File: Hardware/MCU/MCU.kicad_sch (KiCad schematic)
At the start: 36 parts, among them J1 spi0, J10 i2s, J11 USB_C_Receptacle_USB2.0_16P, J2 sp1, J3 sp2, J4 1778612, J5 1778612, J6 1778612, J7 1778612, J8 i2c0, J9 i2c1, SW1 SW_Push, SW2 SW_Push, U1 ESP32-S3-WROOM-1, U2 USBLC6-2P6

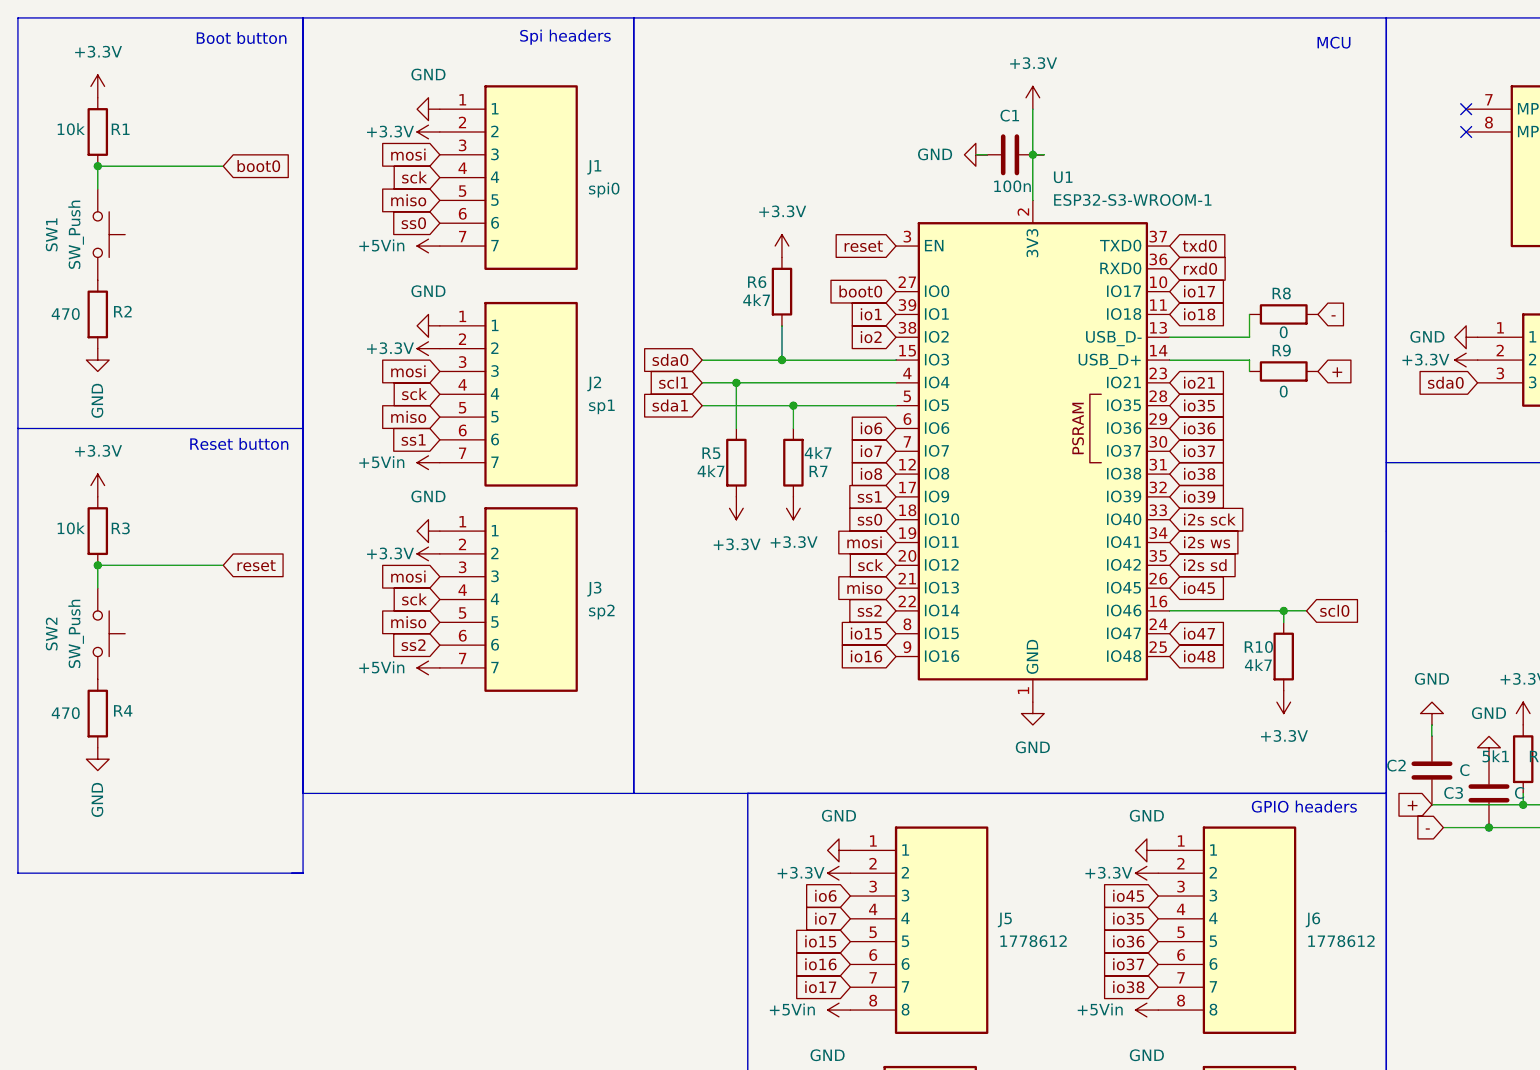
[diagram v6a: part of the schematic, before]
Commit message: boot en reset pin configuratie veranderd, pull up veranderd en capcitoren toegevoegd
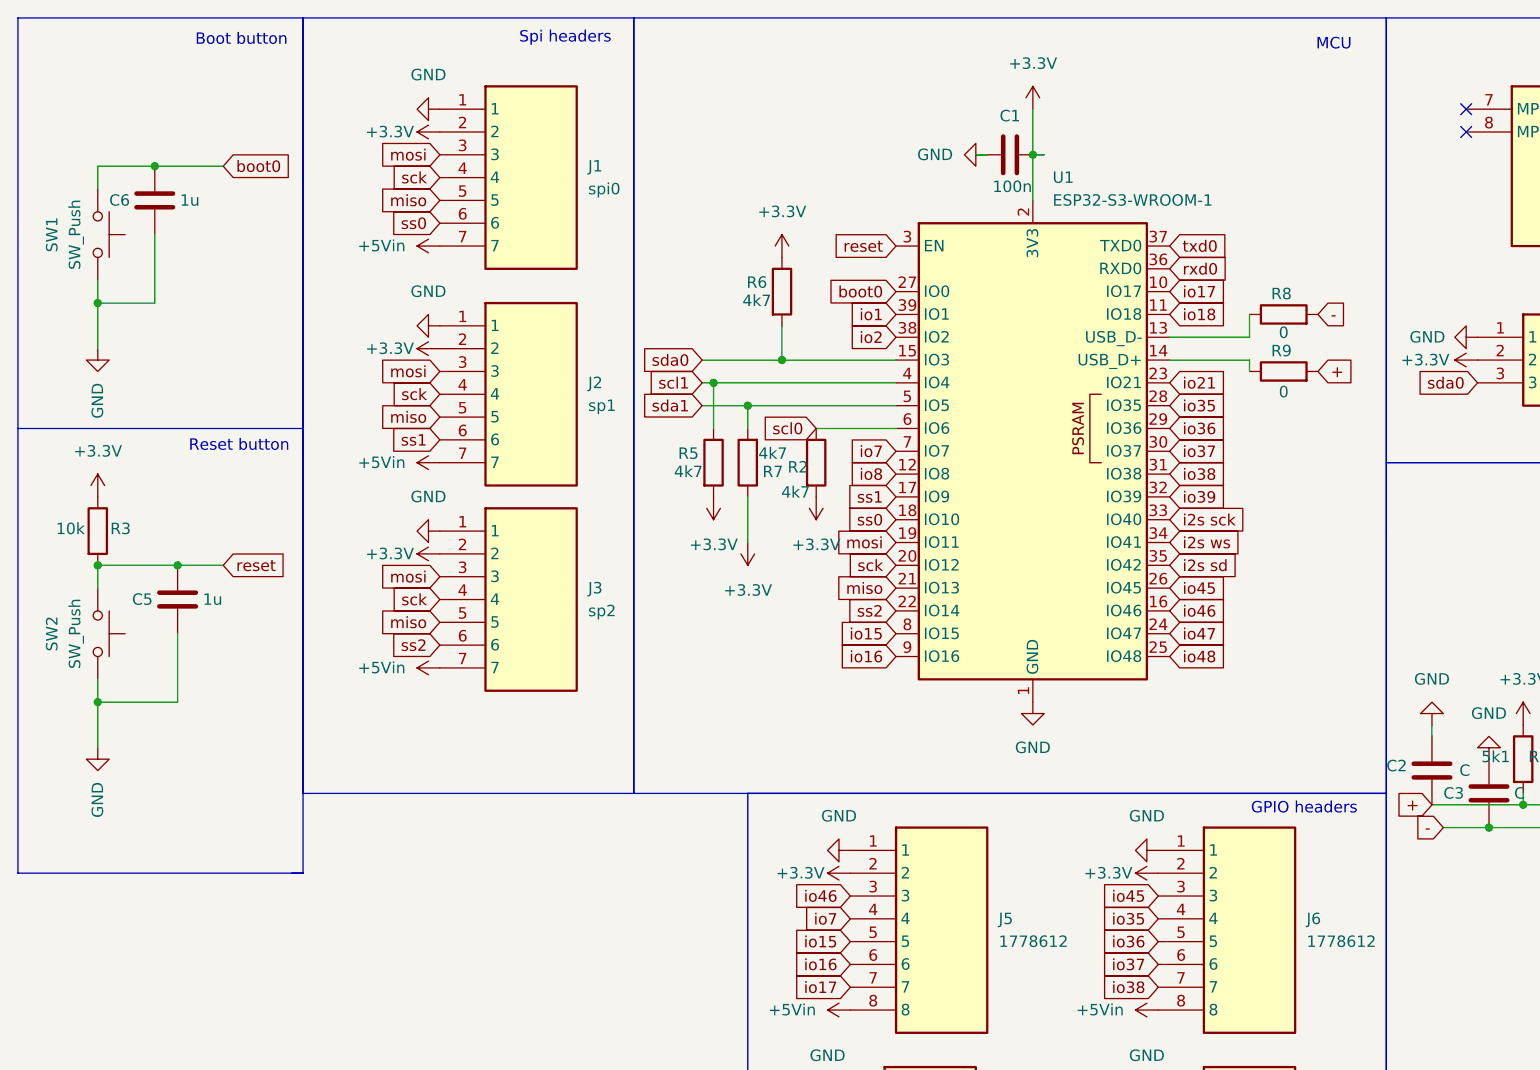
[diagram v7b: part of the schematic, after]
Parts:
- removed R1: 10k, Resistor_SMD:R_1206_3216Metric_Pad1.30x1.75mm_HandSolder, symbol Device:R
- removed R10: 4k7, Resistor_SMD:R_1206_3216Metric_Pad1.30x1.75mm_HandSolder, symbol Device:R
- removed R4: 470, Resistor_SMD:R_1206_3216Metric_Pad1.30x1.75mm_HandSolder, symbol Device:R
- added C5, C6: 1u, Capacitor_SMD:C_1206_3216Metric_Pad1.33x1.80mm_HandSolder, symbol Device:C
- R2: value 470 -> 4k7
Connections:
- net +3.3V: now also R2.2
- net GND: now also SW1.2, SW2.2, C5.2, C6.2; no longer R2.2
- net boot0: now also C6.1
- net reset: now also C5.1
- net scl0: now also R2.1, U1.6 (IO6); no longer U1.16 (IO46)
- net io6 renamed io46
- net io46: now also U1.16 (IO46); no longer U1.6 (IO6)
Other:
- moved on the sheet: R5, R7

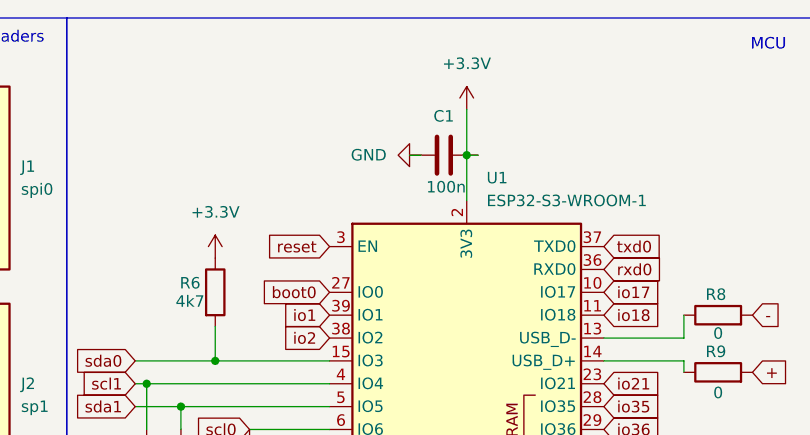
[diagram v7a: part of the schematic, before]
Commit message: new footprint usb-c
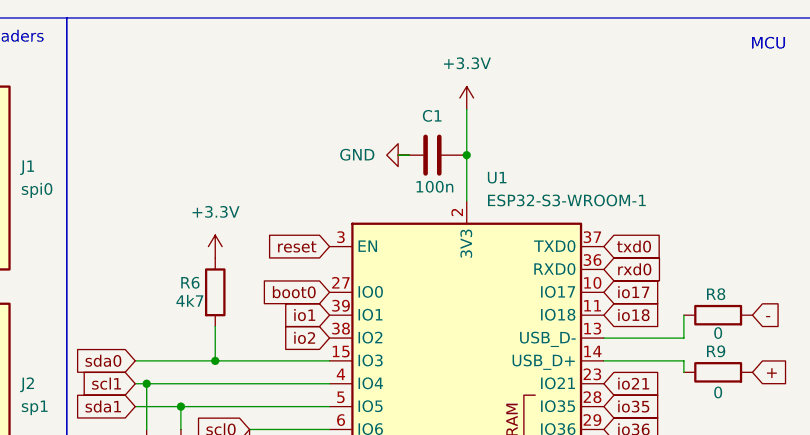
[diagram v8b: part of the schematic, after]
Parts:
- J11: footprint Connector_USB:USB_C_Receptacle_G-Switch_GT-USB-7010ASV -> Connector_USB:USB_C_Receptacle_GCT_USB4105-xx-A_16P_TopMnt_Horizontal
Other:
- moved on the sheet: C1
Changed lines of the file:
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@@
 	(wire
 		(pts
-			(xy 121.92 29.21) (xy 123.19 29.21)
+			(xy 120.65 29.21) (xy 121.92 29.21)
 		)
 		(stroke
@@
 	(wire
 		(pts
-			(xy 128.27 29.21) (xy 129.54 29.21)
-		)
-		(stroke
-			(width 0)
-			(type default)
-		)
-	)
-	(wire
-		(pts
 			(xy 24.13 43.18) (xy 24.13 45.72)
 		)
@@
 			)
 		)
-		(property "Footprint" "Connector_USB:USB_C_Receptacle_G-Switch_GT-USB-7010ASV"
+		(property "Footprint" "Connector_USB:USB_C_Receptacle_GCT_USB4105-xx-A_16P_TopMnt_Horizontal"
 			(at 218.44 99.06 0)
 			(effects
@@
 	(symbol
 		(lib_id "power:GND")
-		(at 123.19 29.21 270)
+		(at 121.92 29.21 270)
 		(unit 1)
 		(exclude_from_sim no)
@@
 		(fields_autoplaced yes)
 		(property "Reference" "#PWR023"
-			(at 116.84 29.21 0)
+			(at 115.57 29.21 0)
 			(effects
 				(font
@@
 		)
 		(property "Value" "GND"
-			(at 119.38 29.2099 90)
+			(at 118.11 29.2099 90)
 			(effects
 				(font
@@
 		)
 		(property "Footprint" ""
-			(at 123.19 29.21 0)
+			(at 121.92 29.21 0)
 			(effects
 				(font
@@
 		)
 		(property "Datasheet" ""
-			(at 123.19 29.21 0)
+			(at 121.92 29.21 0)
 			(effects
 				(font
@@
 		)
 		(property "Description" "Power symbol creates a global label with name \"GND\" , ground"
-			(at 123.19 29.21 0)
+			(at 121.92 29.21 0)
 			(effects
 				(font
@@
 	(symbol
 		(lib_id "Device:C")
-		(at 125.73 29.21 90)
+		(at 124.46 29.21 90)
 		(unit 1)
 		(exclude_from_sim no)
@@
 		(dnp no)
 		(property "Reference" "C1"
-			(at 125.73 24.892 90)
+			(at 124.46 24.892 90)
 			(effects
 				(font
@@
 		)
 		(property "Value" "100n"
-			(at 125.984 32.766 90)
+			(at 124.714 32.766 90)
 			(effects
 				(font
@@
 		)
 		(property "Footprint" "Capacitor_SMD:C_1206_3216Metric_Pad1.33x1.80mm_HandSolder"
-			(at 129.54 28.2448 0)
+			(at 128.27 28.2448 0)
 			(effects
 				(font
@@
 		)
 		(property "Datasheet" "~"
-			(at 125.73 29.21 0)
+			(at 124.46 29.21 0)
 			(effects
 				(font
@@
 		)
 		(property "Description" "Unpolarized capacitor"
-			(at 125.73 29.21 0)
+			(at 124.46 29.21 0)
 			(effects
 				(font
